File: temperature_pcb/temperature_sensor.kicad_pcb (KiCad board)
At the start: 2 copper layers, 167.1 x 67.3 mm, 17 parts, among them J1 Screw_Terminal_01x02, M1 MAX31865-adafruit-module, M10 MAX31865-adafruit-module, M11 MAX31865-adafruit-module, M12 MAX31865-adafruit-module, M13 MAX31865-adafruit-module, M2 MAX31865-adafruit-module, M3 MAX31865-adafruit-module, M4 MAX31865-adafruit-module, M5 MAX31865-adafruit-module, M6 MAX31865-adafruit-module, M7 MAX31865-adafruit-module, M8 MAX31865-adafruit-module, M9 MAX31865-adafruit-module

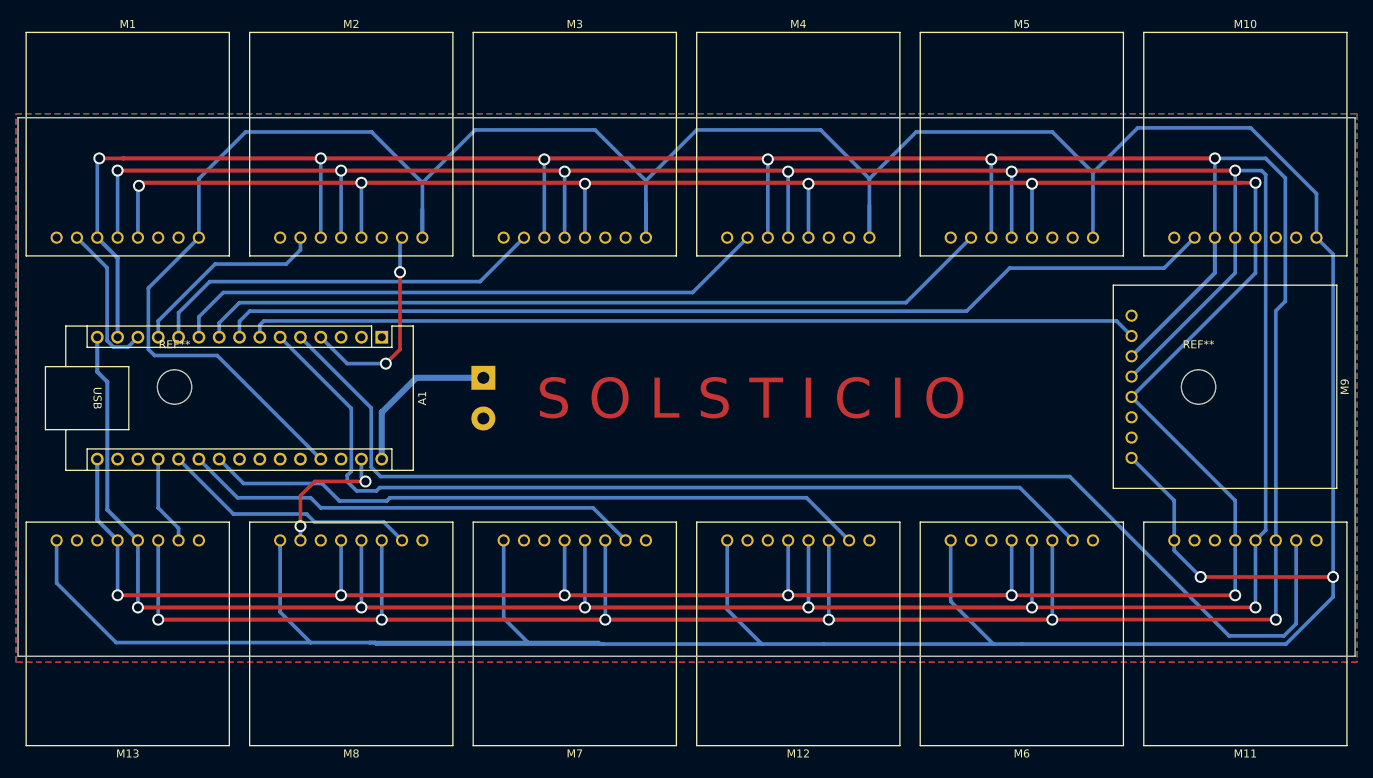
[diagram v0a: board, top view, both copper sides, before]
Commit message: fixed max31865 footprint pinout, unrouted all the max in the temperature_sensor pcb
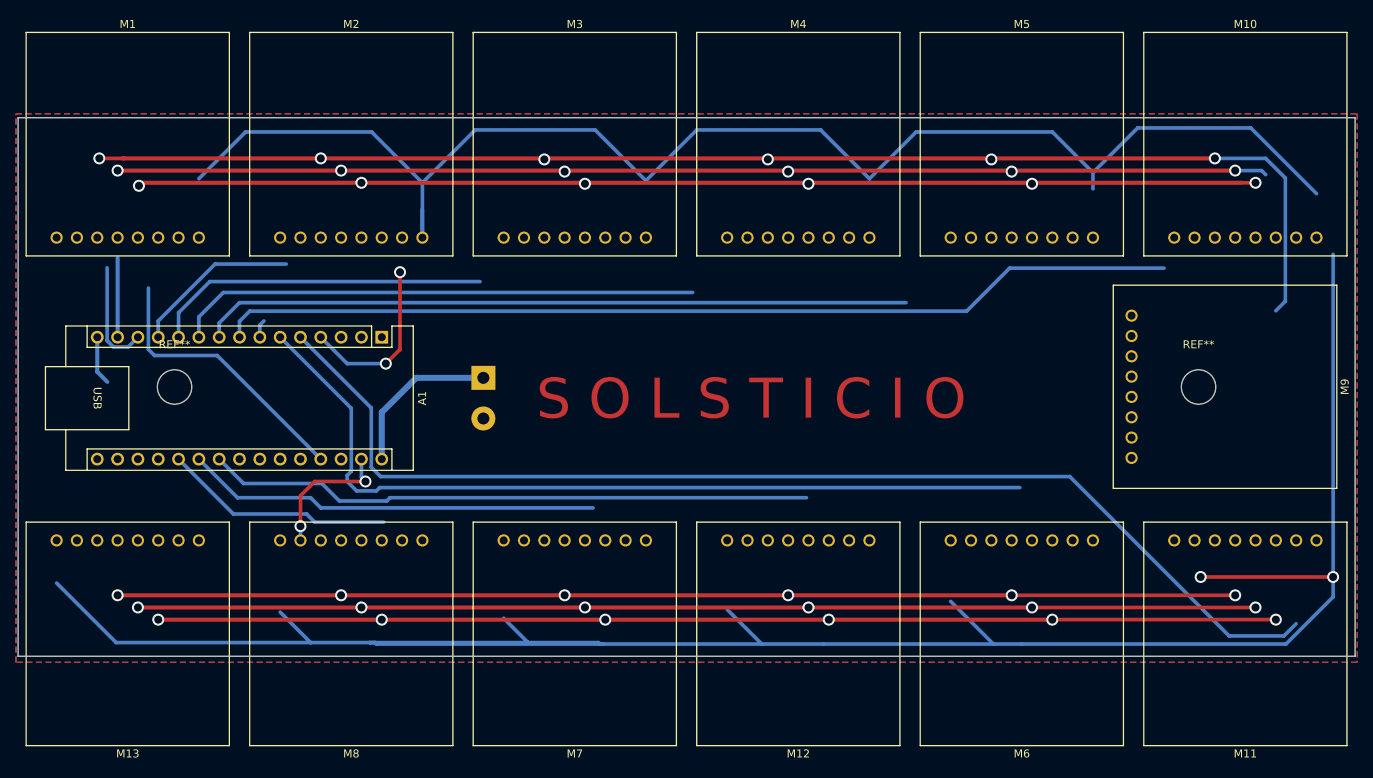
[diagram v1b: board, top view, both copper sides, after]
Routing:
- net +5V: track 603.4 -> 34.9 mm, vias 2 -> 0
- net MOSI: track 486.6 -> 176.9 mm, vias 12 -> 6
- net unconnected-(M13-RDY-Pad1): track 0.00 -> 277.2 mm, vias 0 -> 2
- net MISO: track 480.5 -> 289.5 mm
- net unconnected-(M2-RDY-Pad1): track 0.00 -> 178.0 mm
- net SCK: track 422.4 -> 279.8 mm
- net unconnected-(M13-3V3-Pad6): track 0.00 -> 139.7 mm, vias 0 -> 6
- net CS2: track 111.5 -> 2.24 mm
- net CS4: track 100.2 -> 88.7 mm
- net CS9: track 11.2 -> 0.00 mm
- net CS0: track 155.3 -> 144.9 mm
- net CS5: track 75.2 -> 65.5 mm
- net CS1: track 116.0 -> 106.7 mm
- net CS6: track 50.1 -> 42.3 mm
- net CS12: track 83.3 -> 75.7 mm
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
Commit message: routed new pads
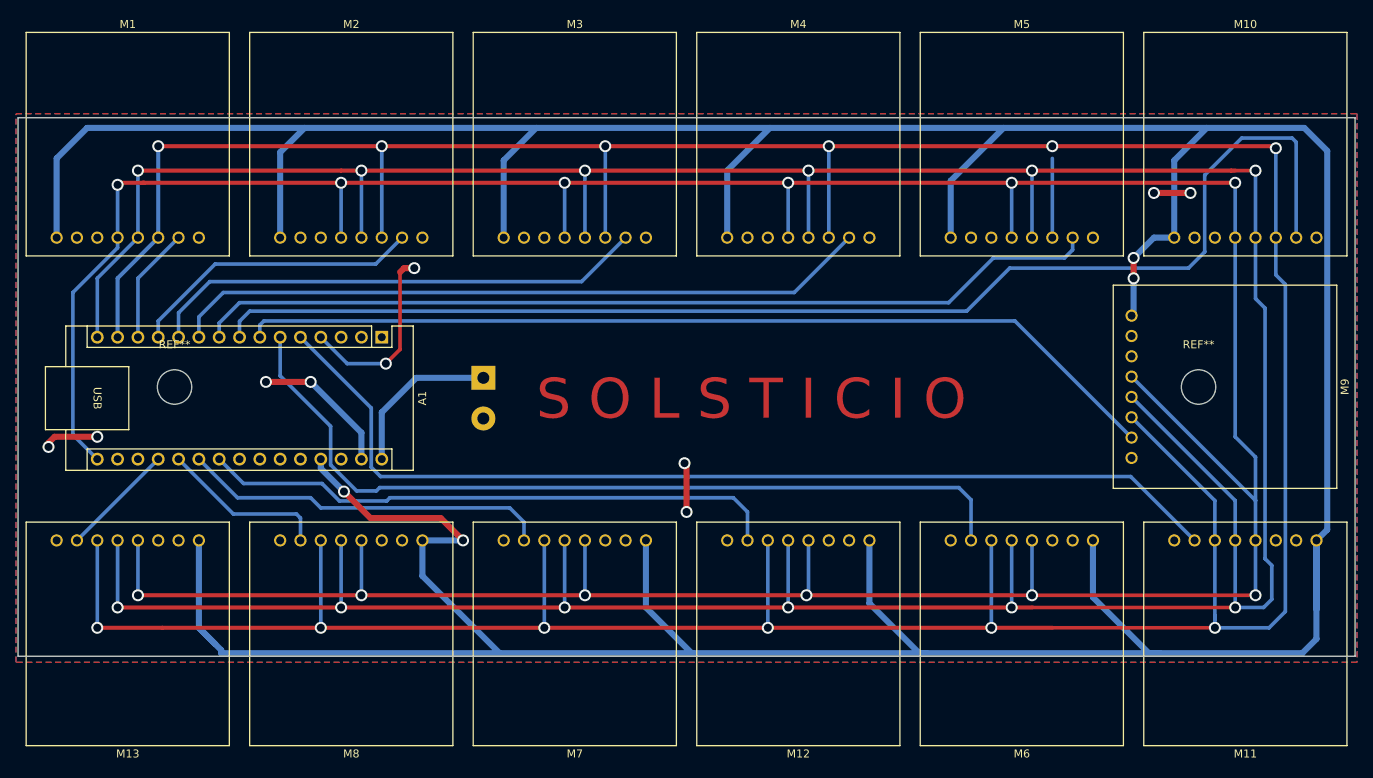
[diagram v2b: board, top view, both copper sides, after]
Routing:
- net +5V: track 34.9 -> 587.5 mm, vias 0 -> 4
- net MOSI: track 176.9 -> 506.5 mm, vias 6 -> 12
- net unconnected-(M13-RDY-Pad1): track 277.2 -> 0.00 mm, vias 2 -> 0
- net MISO: track 289.5 -> 469.4 mm
- net unconnected-(M2-RDY-Pad1): track 178.0 -> 0.00 mm
- net SCK: track 279.8 -> 454.0 mm
- net unconnected-(M13-3V3-Pad6): track 139.7 -> 0.00 mm, vias 6 -> 0
- net CS2: track 2.24 -> 116.7 mm
- net CS3: track 120.3 -> 161.3 mm
- net CS4: track 88.7 -> 113.8 mm
- net CS5: track 65.5 -> 87.9 mm
- net CS6: track 42.3 -> 62.8 mm
- net GND: track 39.1 -> 59.3 mm, vias 4 -> 10
- net CS0: track 144.9 -> 126.6 mm
- net CS7: track 21.3 -> 36.8 mm
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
